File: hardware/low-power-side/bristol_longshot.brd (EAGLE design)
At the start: 38 x 46.1 mm, 80 parts, among them U1 SAM_D20E, U10 ADP1607ACPZN-R7, U11 TPS73118DBVT, U12 TPS73118DBVT, U14 SIT1552, U15 LIS2DH, U16 SIT1552, U2 SI4060, U3 SE880, U4 SST25WF040BT-40I/NP, U5 TG-5006CJ, U6 TG-5006CJ, U7 TPS3123, U8 SN74LVC1G32DCKR, U9 MS5607-02BA03

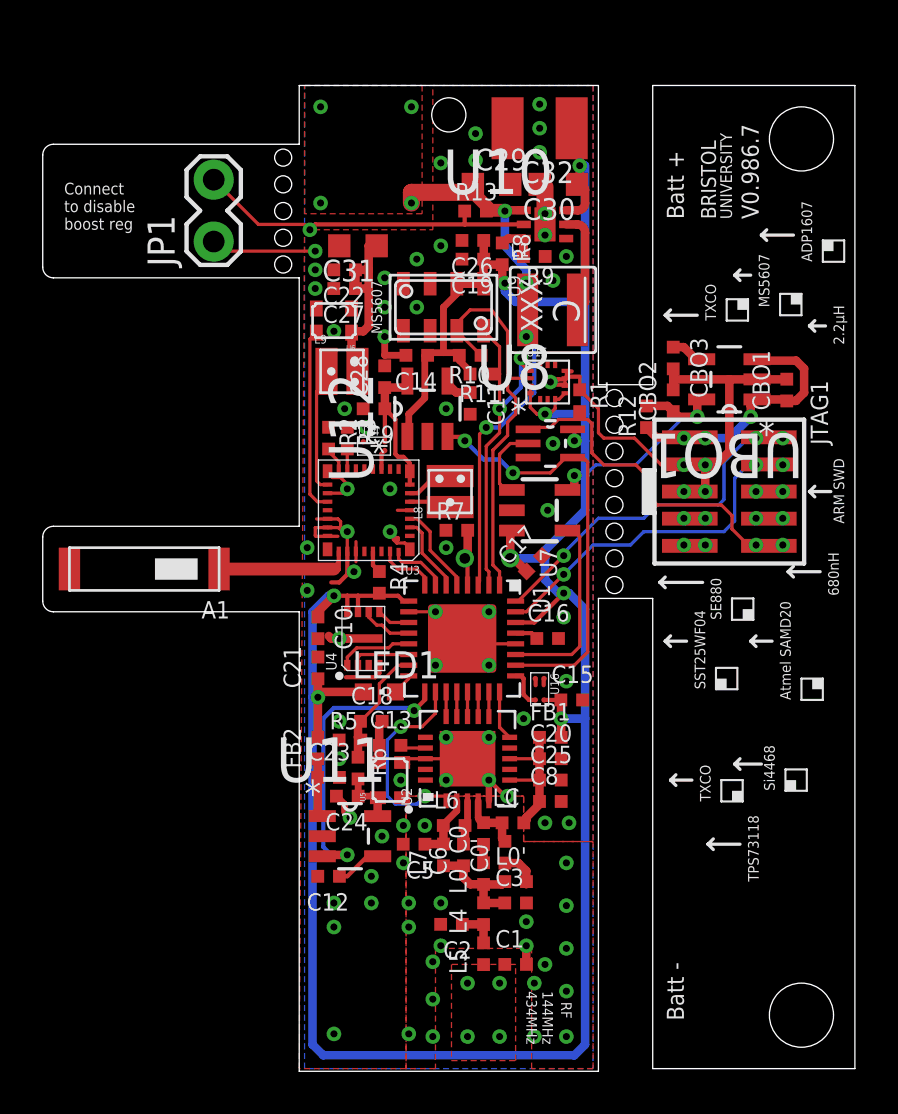
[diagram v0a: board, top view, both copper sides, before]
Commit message: [low-power] v0.986.8. Changed memory pads, GPS LDO and specified SAMD20E18A-MN with more flash and higher grade packaging
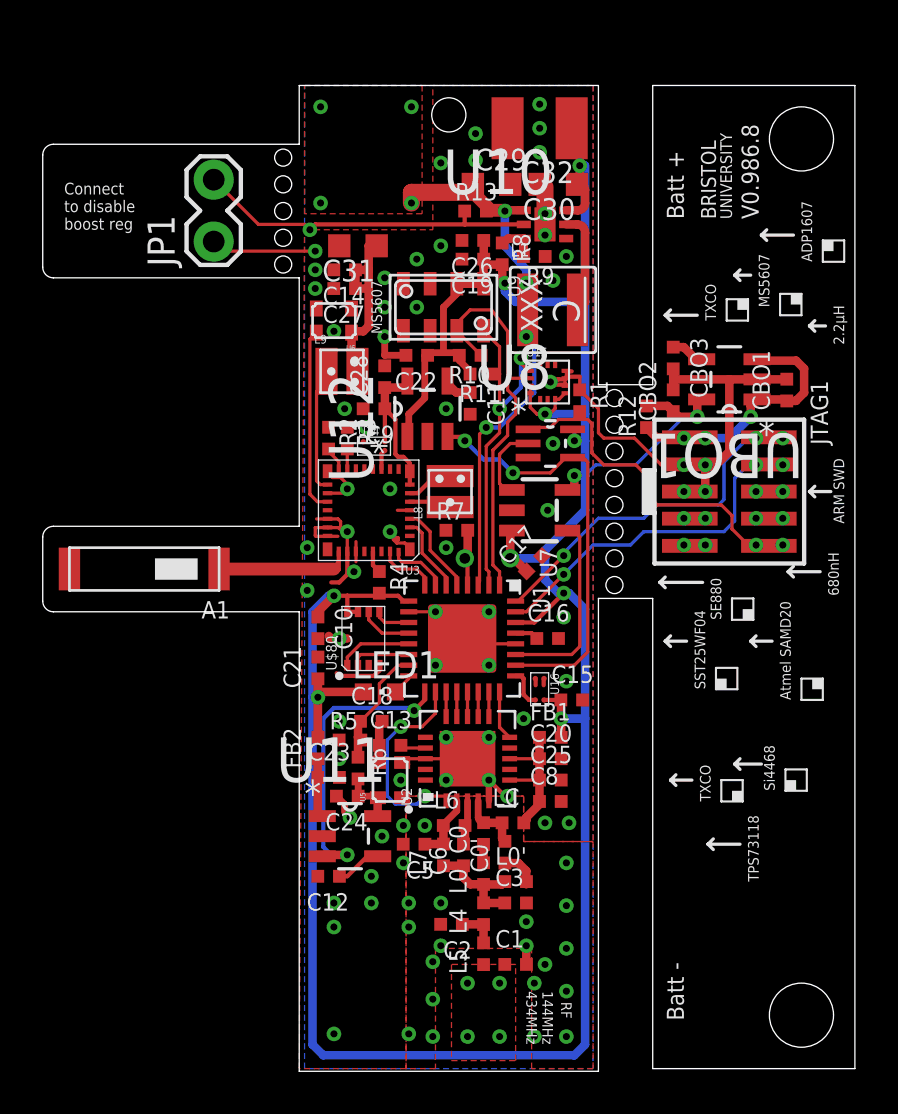
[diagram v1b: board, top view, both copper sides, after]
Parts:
- C11: value 10nF -> DNP
- U12: value TPS73118DBVT -> MIC94310-GYM5
- moved C14 5.23 mm to (14.1, 37.4)
- moved C22 5.23 mm to (17.5, 33.4)
- renumbered U4 to U$80
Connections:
- net 1.8V: now also C22.1; no longer C14.1
- net GND: no longer U$80.P$9
- net TCXO_VDD1: now also C14.1; no longer C22.1
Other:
- board text added: "V0.986.8"
- board text removed: "V0.986.7"

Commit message: [low-power] |v0.987.0|Low Power. Added 32kHz TCXO RC filters, replaced GPS LDO with MOSFET, remove IMU, vreg on b/out, update SE880 footprint, Watchdog, Radio, filter design
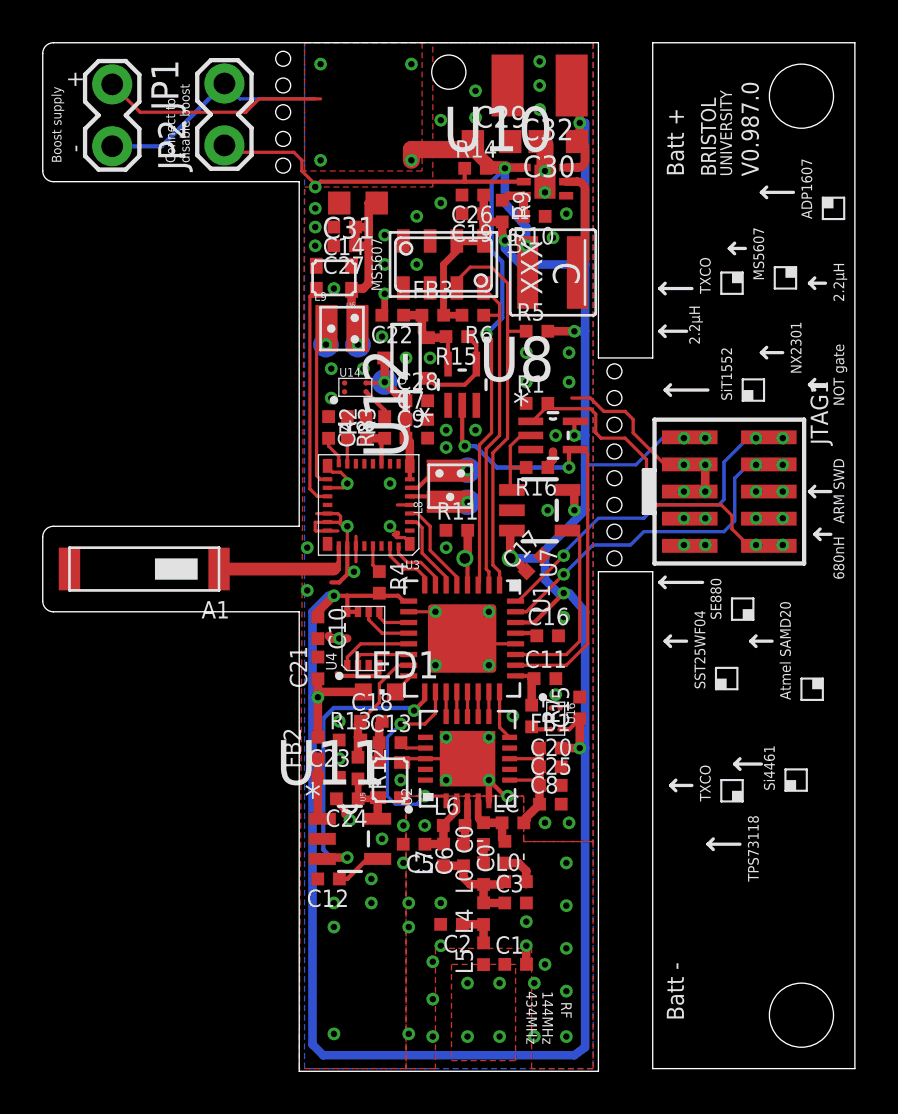
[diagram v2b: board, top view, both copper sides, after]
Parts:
- removed CBO1, CBO2: 1µF, microbuilder_v3:_0402@2
- removed CBO3: 10nF, microbuilder_v3:_0402@2
- removed U15: LIS2DH, fbri:LIS2DH
- removed UBO1: TPS73118DBVT, TPS73118DVBT:SOT95P280X145-5N
- added C4: 15pF, microbuilder_v3:_0402
- added C7: 100nF, microbuilder_v3:_0402
- added FB3: (no value), microbuilder_v3:_0402@1
- added JP2: (no value), SparkFun:1X02_LOCK
- added Q1: NX2301P, nxp:SOT23
- added R14: 100kΩ, microbuilder_v3:_0402
- added R15, R16: 1MΩ, microbuilder_v3:_0402
- C0, C1, C10, C12, C13, C14, C15, C16, C17, C18, C19, C2, C20, C21, C22, C23, C24, C25, C26, C27, C3, C5, C6, C8, C9: device microbuilder_v3:_0402@2 -> microbuilder_v3:_0402
- C0': value 15pF -> DNP; device microbuilder_v3:_0402@2 -> microbuilder_v3:_0402
- C11: value DNP -> 15pF; device microbuilder_v3:_0402@2 -> microbuilder_v3:_0402
- C28: value 1µF -> 2.2µF; device microbuilder_v3:_0402@2 -> microbuilder_v3:_0402
- L0, L4, L5, L6, L7: device microbuilder_v3:_0402@1 -> microbuilder_v3:_0402
- L0': value 56nH -> DNP; device microbuilder_v3:_0402@1 -> microbuilder_v3:_0402
- LC: value 220nH -> 470nH; device microbuilder_v3:_0402@1 -> microbuilder_v3:_0402
- R10, R11, R13: value 10kΩ -> 100kΩ
- R12: value 0Ω -> 100kΩ
- R5, R6, R7: value 100kΩ -> 10kΩ
- R8: value 43kΩ -> 10kΩ
- R9: value 100kΩ -> 43kΩ
- U12: value MIC94310-GYM5 -> 74LVC1G04GW; device TPS73118DVBT:SOT95P280X145-5N -> 74LVC1G04GW_inverter:SOT65P210X110-5N
- U2: value SI4060 -> SI4461
- U7: value TPS3123 -> ADM6823WYRJZ
- moved R13 25.4 mm to (14.4, 15.4)
- moved R6 21.9 mm to (20.1, 35.2), turned to 180 degrees
- moved R12 21.3 mm to (14.8, 14.1), turned to 270 degrees
- moved R5 21.0 mm to (23.1, 34.5)
- moved C11 13.3 mm to (23.5, 18.2), turned to 0 degrees
- moved R8 9.81 mm to (16.0, 30.0), turned to 90 degrees
- moved R7 9.37 mm to (22.9, 16.5), turned to 270 degrees
- moved JP1 8.46 mm to (3.25, 45.9), turned to 270 degrees
- moved R11 7.40 mm to (19.4, 25.2), turned to 0 degrees
- moved R10 7.16 mm to (23.0, 39.9)
- moved U14 2.89 mm to (14.6, 31.9)
- moved R9 2.60 mm to (21.5, 40.1), turned to 270 degrees
- moved C9 2.43 mm to (17.5, 29.5), turned to 0 degrees
- moved C22 2.19 mm to (16.4, 35.2)
- moved C19 2.12 mm to (20.1, 40.0)
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- renumbered U$80 to U4
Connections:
- net TCXO_VDD1 renamed SE_TCXO_VDD
- removed net GPS_REG_NR: C11.1, U12.4
- removed net JTAG_VIN: CBO1.1, JTAG1.1, R12.1, UBO1.1, UBO1.3
- removed net JTAG_VREG_NR: CBO3.1, UBO1.4
- new net GPS_VDD_SWITCHED: C28.1, C7.1, C9.1, Q1.3, U14.3, U3.8, U3.9
- new net LF_CLOCK_OUT: R7.2, U16.2
- new net RESET: Q1.1, R15.1, U12.4
- new net SE800_LF_OUT: R8.2, U14.2
- net !RESET: now also U12.2; no longer U12.3
- net 1.2V: now also JP1.1, R14.2; no longer R13.2
- net 1.8V: now also FB3.2, JTAG1.1, R5.2, R6.2, R9.2; no longer C22.1, CBO2.1, R10.2, R11.2, R12.2, R8.2, U12.1, U15.3, U15.4, U15.7, U15.8, UBO1.5
- net BOOST_EN: now also JP2.1, R14.1; no longer JP1.2, R13.1
- net EXT_THERMISTOR_SENSE: now also R11.2; no longer R7.2
- net FB: now also R10.2, R9.1; no longer R8.1, R9.2
- net GND: now also C4.2, C7.2, JP1.2, JP2.2, R10.1, R11.1, R13.1, R16.1, U12.3; no longer CBO1.2, CBO2.2, CBO3.2, JP1.1, R5.1, R7.1, R9.1, U12.2, U15.10, U15.11, U15.9, UBO1.2
- net GPS_VDD: now also C22.1, FB3.1, Q1.2, R15.2; no longer C28.1, C9.1, U14.3, U3.8, U3.9
- net LF_CLOCK: now also C11.1, R7.1; no longer U16.2
- net RTC_XI: now also C4.1, R8.1; no longer U14.2
- net SAM_XOSC: now also R12.1, R13.2; no longer R5.2, R6.1
- net SCL: now also R6.1; no longer R11.1, U15.1
- net SDA: now also R5.1; no longer R10.1, U15.2
- net TCXO_VDD: now also R12.2; no longer R6.2
- net WDI!RESET: now also R16.2
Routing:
- net 1.2V: track 26.4 -> 43.6 mm, vias 8 -> 7
- net JTAG_VIN: track 12.6 -> 0.00 mm, vias 3 -> 0
- net 1.8V: track 144.2 -> 133.2 mm, vias 11 -> 12
- net GND: track 66.8 -> 57.5 mm, vias 84 -> 93
- net GPS_VDD_SWITCHED: track 0.00 -> 7.12 mm, vias 0 -> 1
- net RESET: track 0.00 -> 4.51 mm
- net GPS_VDD: track 8.10 -> 4.23 mm
- net SE_VCC_TCXO: track 5.90 -> 7.95 mm, vias 0 -> 1
- net !RESET: track 20.2 -> 21.9 mm
- net SE_TCXO_CLK: track 8.65 -> 10.4 mm
- net JTAG_VREG_NR: track 1.56 -> 0.00 mm
- net SE800_LF_OUT: track 0.00 -> 1.52 mm
- net GPS_REG_NR: track 1.36 -> 0.00 mm
- net RTC_XI: track 0.93 -> 2.22 mm
- net SCL: track 16.8 -> 15.5 mm, vias 2 -> 0
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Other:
- board size 38 x 46.1 mm -> 38 x 48.1 mm
- board text added: "+"
- board text added: "-"
- board text added: "Boost supply"
- board text added: "Connect to disable boost"
- board text added: "NOT gate"
- board text added: "NX2301"
- board text added: "Si4461"
- board text added: "SiT1552"
- board text added: "V0.987.0"
- board text removed: "Connect to disable boost reg"
- board text removed: "Si4468"
- board text removed: "V0.986.8"

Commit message: [low-power] |v0.987.1|Low Power. Switch LF Clock to XOSC32K pin from GCLK_IO[0]. Allows feed to any GCLK. Bit-bang i2c instead
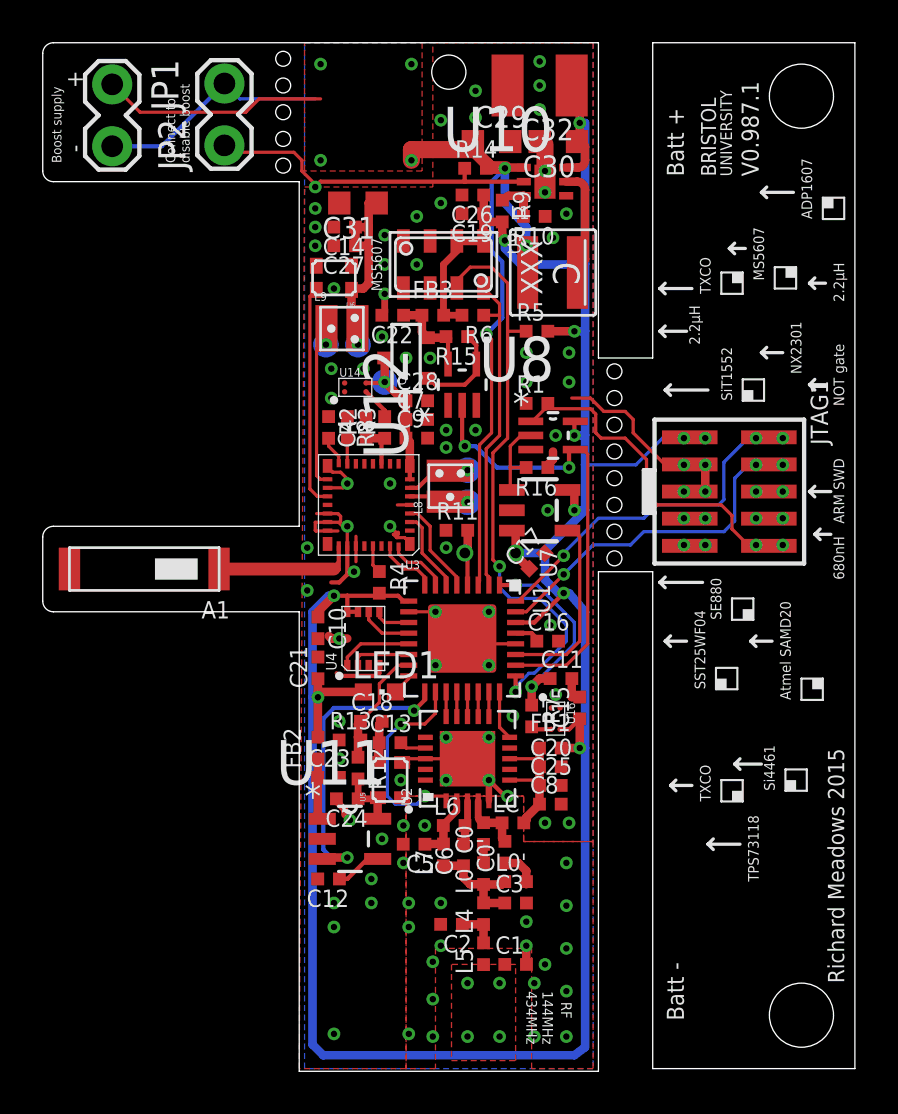
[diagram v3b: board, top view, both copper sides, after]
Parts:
- moved C11 0.75 mm to (24.2, 18.2)
- moved C16 0.25 mm to (23.6, 20.0)
- moved C17 0.18 mm to (23.1, 23.8)
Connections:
- net SCL renamed SCL_BITB
- removed net SDA: R5.1, U1.1, U9.7
- new net SDA_BITB: R5.1, U1.25, U9.7
- net LF_CLOCK: now also U1.1; no longer U1.25
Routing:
- net SDA_BITB: track 0.00 -> 27.9 mm, vias 0 -> 2
- net SDA: track 18.9 -> 0.00 mm
- net LF_CLOCK: track 2.29 -> 9.95 mm, vias 0 -> 2
- net GND: track 57.5 -> 58.7 mm
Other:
- board text added: "V0.987.1"
- board text removed: "V0.987.0"
